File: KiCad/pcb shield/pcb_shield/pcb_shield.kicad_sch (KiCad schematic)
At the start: 30 parts, among them J1 , J10 Motor Conn L, J11 Motor Conn R, J12 Endstop X, J13 Endstop Y, J14 Barrel_Jack, J15 Add Conn, J16 Add Conn, J17 Add Conn, J18 Add Conn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

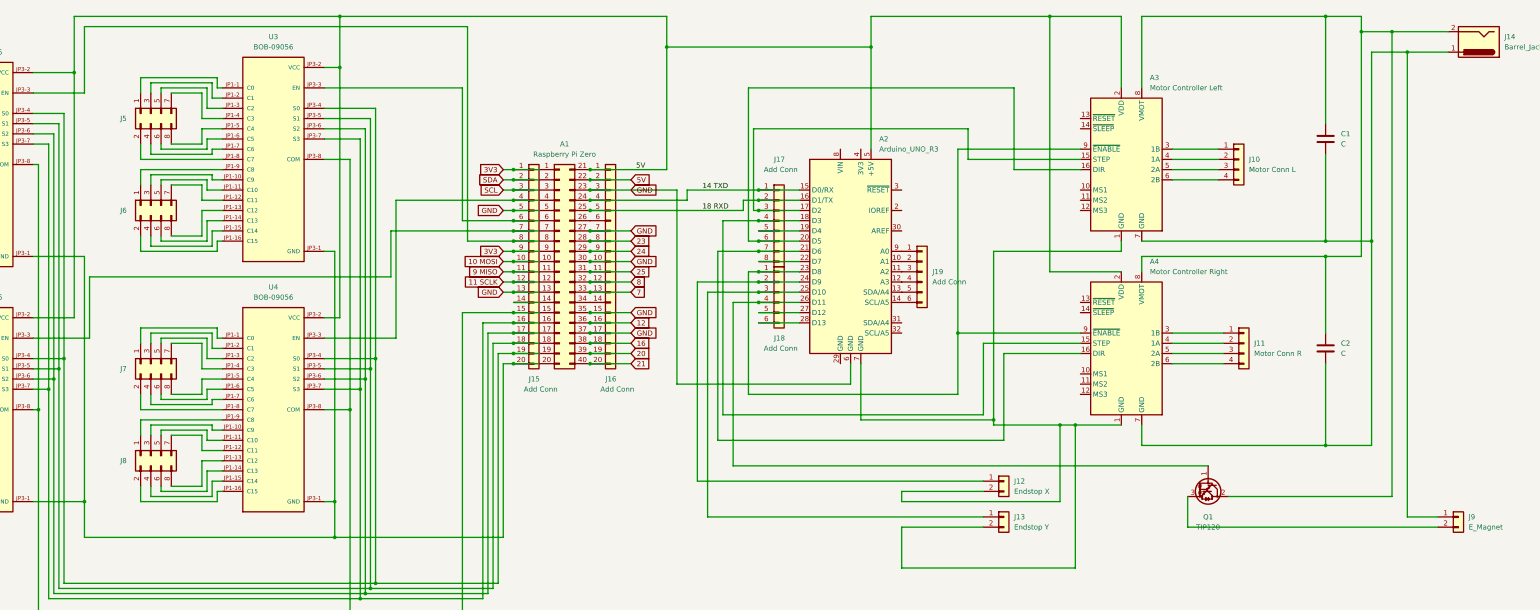
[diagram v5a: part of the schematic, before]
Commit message: working on PCB and creating manufacturing files
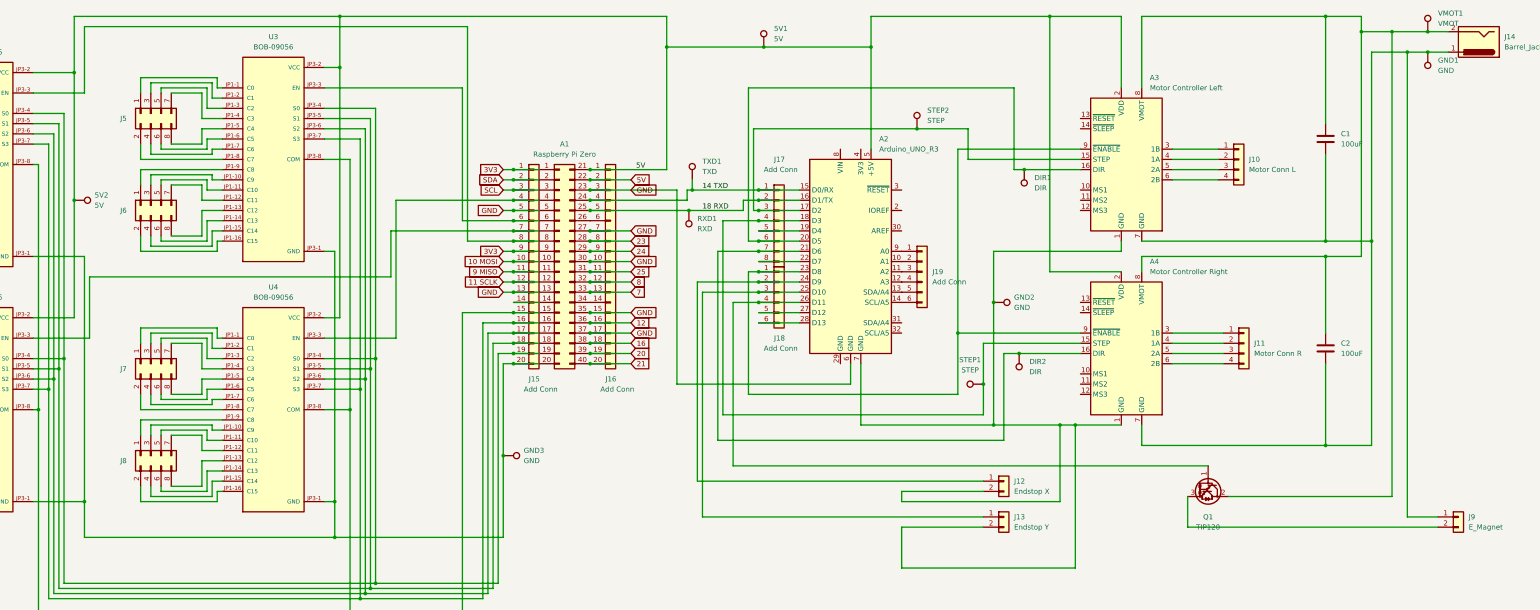
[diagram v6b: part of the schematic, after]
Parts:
- added 5V1, 5V2: 5V, TestPoint:TestPoint_Pad_D2.0mm, symbol Connector:TestPoint
- added DIR1, DIR2: DIR, TestPoint:TestPoint_Pad_D2.0mm, symbol Connector:TestPoint
- added GND1, GND2, GND3: GND, TestPoint:TestPoint_Pad_D2.0mm, symbol Connector:TestPoint
- added RXD1: RXD, TestPoint:TestPoint_Pad_D2.0mm, symbol Connector:TestPoint
- added STEP1, STEP2: STEP, TestPoint:TestPoint_Pad_D2.0mm, symbol Connector:TestPoint
- added TXD1: TXD, TestPoint:TestPoint_Pad_D2.0mm, symbol Connector:TestPoint
- added VMOT1: VMOT, TestPoint:TestPoint_Pad_D2.0mm, symbol Connector:TestPoint
- C1, C2: value C -> 100uF
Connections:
- net 14 TXD: now also TXD1.1
- net 18 RXD: now also RXD1.1
- net 5V: now also 5V1.1, 5V2.1
- net at A3.7 (GND), A4.7 (GND), C1.2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: now also GND1.1
- net at A2.17 (D2), A3.15 (STEP), J17.3 (Pin_3): now also STEP2.1
- net at A2.18 (D3), A4.15 (STEP), J17.4 (Pin_4): now also STEP1.1
- net at A2.20 (D5), A3.16 (DIR), J17.6 (Pin_6): now also DIR1.1
- net at A2.21 (D6), A4.16 (DIR), J17.7 (Pin_7): now also DIR2.1
- net at A2.7 (GND), A3.1 (GND), A4.1 (GND)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: now also GND2.1
- net at A3.8 (VMOT), A4.8 (VMOT), C1.1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: now also VMOT1.1
- net at A1.20 (Pin_20), J15.20 (Pin_20), U1.JP3-1 (GND)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: now also GND3.1
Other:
- company: (none) -> Gymnasium Dresden-Plauen
- title: (none) -> Automatic Chess PCB

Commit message: make files for hackclub pcb grant
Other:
- company: Gymnasium Dresden-Plauen -> (none)
- moved on the sheet: J14
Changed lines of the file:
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@@
     (date "2025-04-09")
     (rev "1.0")
-    (company "Gymnasium Dresden-Plauen")
     (comment 1 "Author: Felix Wittwer")
   )
@@
     (stroke (width 0) (type default) (color 0 0 0 0))
   )
-  (wire (pts (xy 414.02 34.29) (xy 419.1 34.29))
+  (wire (pts (xy 414.02 34.29) (xy 415.29 34.29))
     (stroke (width 0) (type default) (color 0 0 0 0))
   )
@@
     (stroke (width 0) (type default) (color 0 0 0 0))
   )
-  (wire (pts (xy 414.02 29.21) (xy 419.1 29.21))
+  (wire (pts (xy 414.02 29.21) (xy 415.29 29.21))
     (stroke (width 0) (type default) (color 0 0 0 0))
   )
@@
     (pin "1")
   )
-  (symbol (lib_id "Connector:Barrel_Jack") (at 426.72 31.75 180) (unit 1)
+  (symbol (lib_id "Connector:Barrel_Jack") (at 422.91 31.75 180) (unit 1)
     (in_bom yes) (on_board yes) (fields_autoplaced)
-    (property "Reference" "J14" (id 0) (at 433.07 30.4799 0)
+    (property "Reference" "J14" (id 0) (at 429.26 30.4799 0)
       (effects (font (size 1.27 1.27)) (justify right))
     )
-    (property "Value" "Barrel_Jack" (id 1) (at 433.07 33.0199 0)
+    (property "Value" "Barrel_Jack" (id 1) (at 429.26 33.0199 0)
       (effects (font (size 1.27 1.27)) (justify right))
     )
-    (property "Footprint" "TerminalBlock_Phoenix:TerminalBlock_Phoenix_MKDS-1,5-2_1x02_P5.00mm_Horizontal" (id 2) (at 425.45 30.734 0)
-      (effects (font (size 1.27 1.27)) hide)
-    )
-    (property "Datasheet" "~" (id 3) (at 425.45 30.734 0)
-      (effects (font (size 1.27 1.27)) hide)
-    )
+    (property "Footprint" "TerminalBlock_Phoenix:TerminalBlock_Phoenix_MKDS-1,5-2_1x02_P5.00mm_Horizontal" (id 2) (at 421.64 30.734 0)
+      (effects (font (size 1.27 1.27)) hide)
+    )
+    (property "Datasheet" "~" (id 3) (at 421.64 30.734 0)
+      (effects (font (size 1.27 1.27)) hide)
+    )
